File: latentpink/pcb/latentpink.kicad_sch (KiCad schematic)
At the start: 0 parts

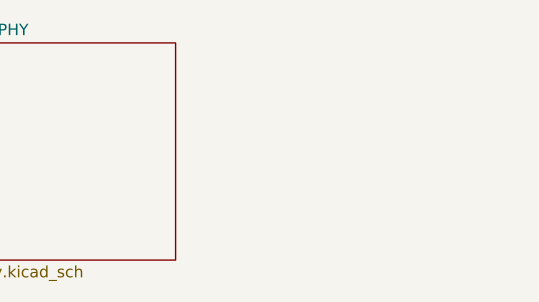
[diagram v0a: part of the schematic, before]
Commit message: Continued initial schematic capture and floorplanning
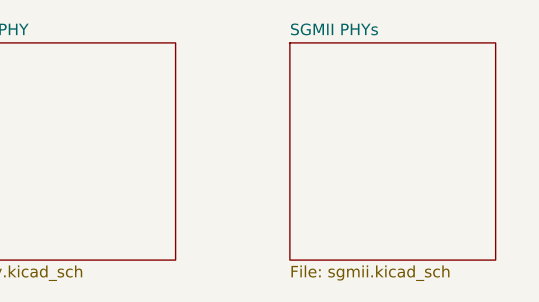
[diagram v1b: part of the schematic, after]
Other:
- added sheet SGMII PHYs (sgmii.kicad_sch)

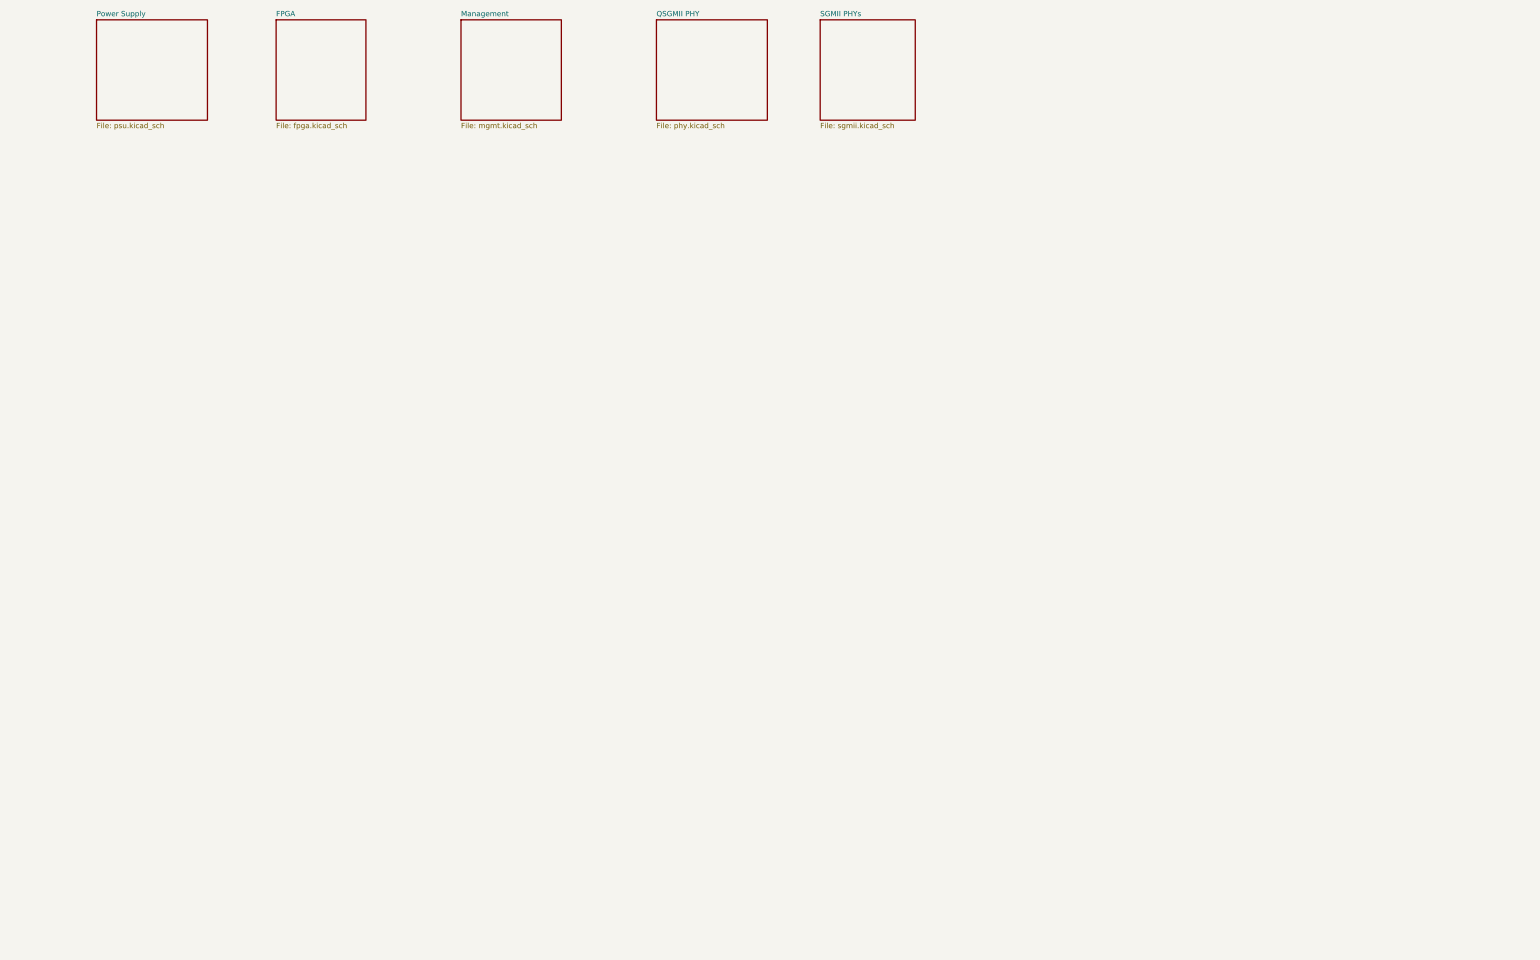
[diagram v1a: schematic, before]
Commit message: Continued initial schematic capture
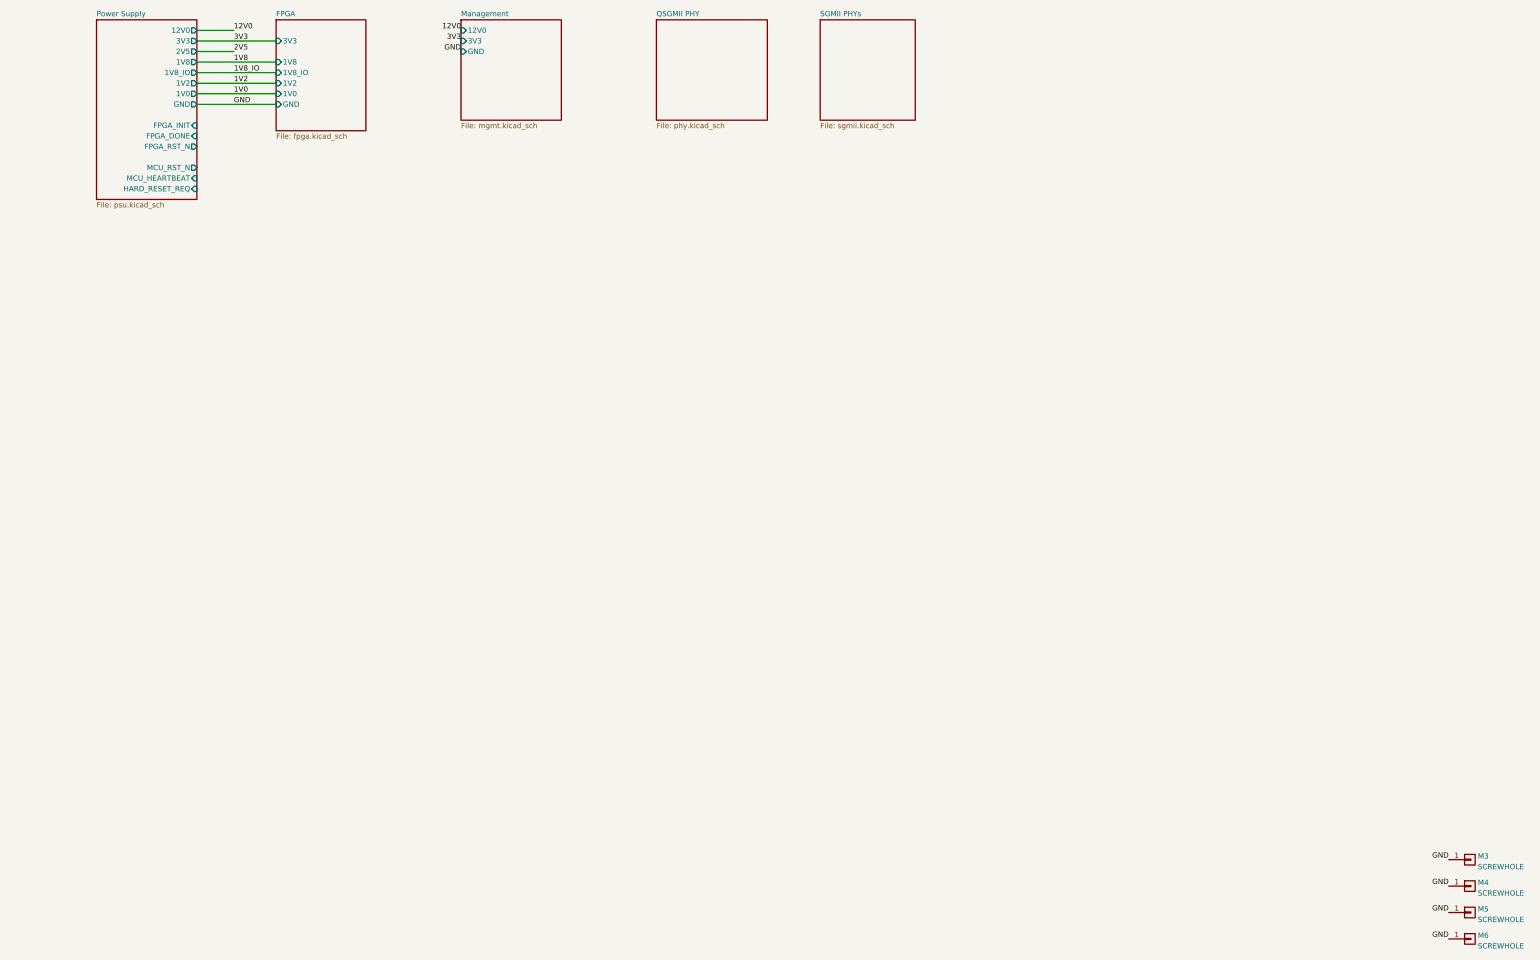
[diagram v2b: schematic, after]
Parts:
- added M3, M4, M5, M6: SCREWHOLE, azonenberg_pcb:MECHANICAL_CLEARANCEHOLE_4_40, symbol conn:CONN_01X01
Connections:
- new net GND: M3.1 (P1), M4.1 (P1), M5.1 (P1), M6.1 (P1)
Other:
- sheet FPGA ports: added 1V0, 1V2, 1V8, 1V8_IO, 3V3, GND; removed none
- sheet Management ports: added 12V0, 3V3, GND; removed none
- sheet Power Supply ports: added 12V0, 1V0, 1V2, 1V8, 1V8_IO, 2V5, 3V3, FPGA_DONE, FPGA_INIT, FPGA_RST_N, GND, HARD_RESET_REQ, MCU_HEARTBEAT, MCU_RST_N; removed none

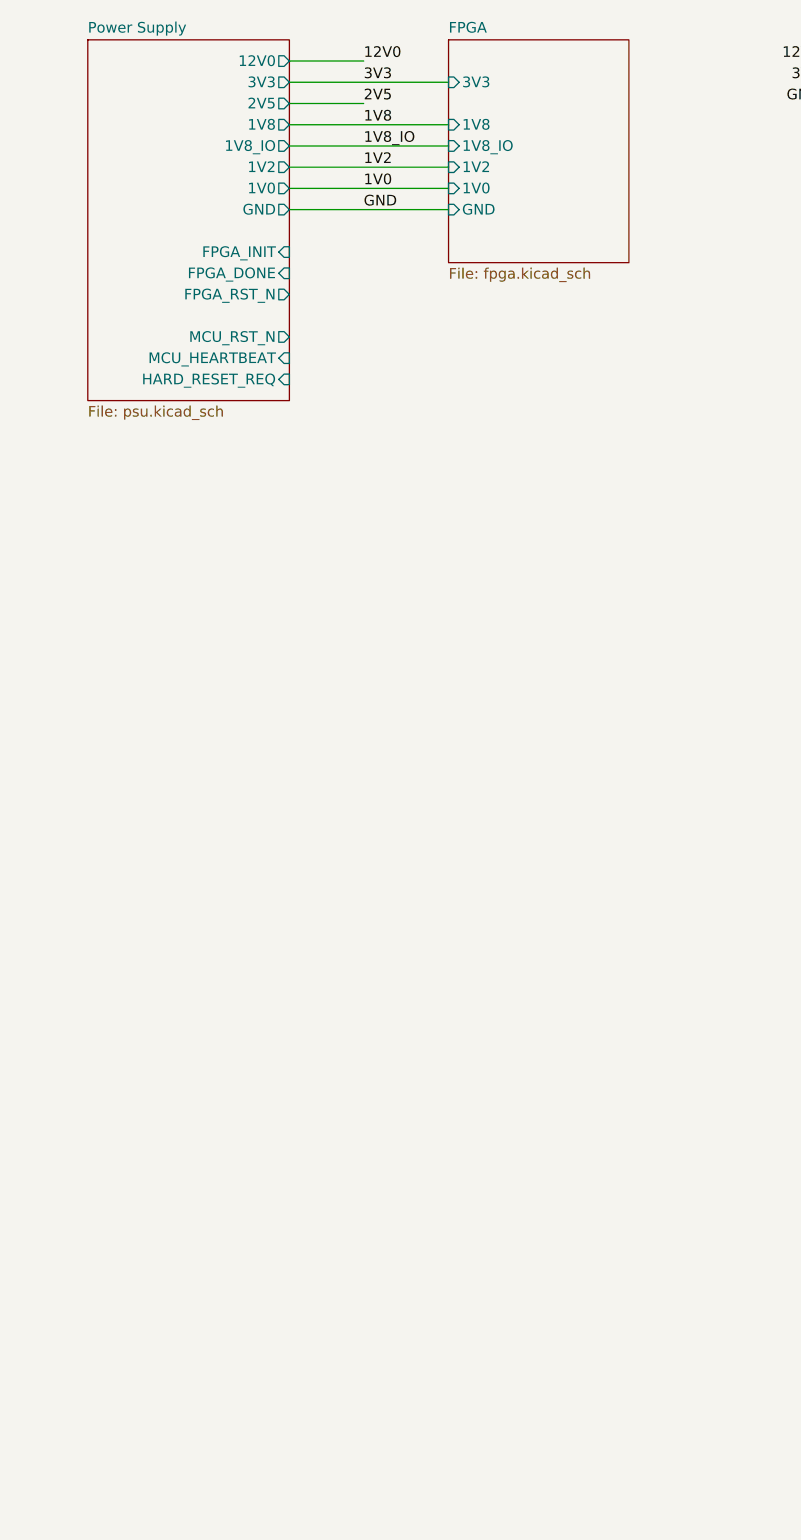
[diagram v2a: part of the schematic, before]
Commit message: Continued work on schematic, mostly power supply and QDR
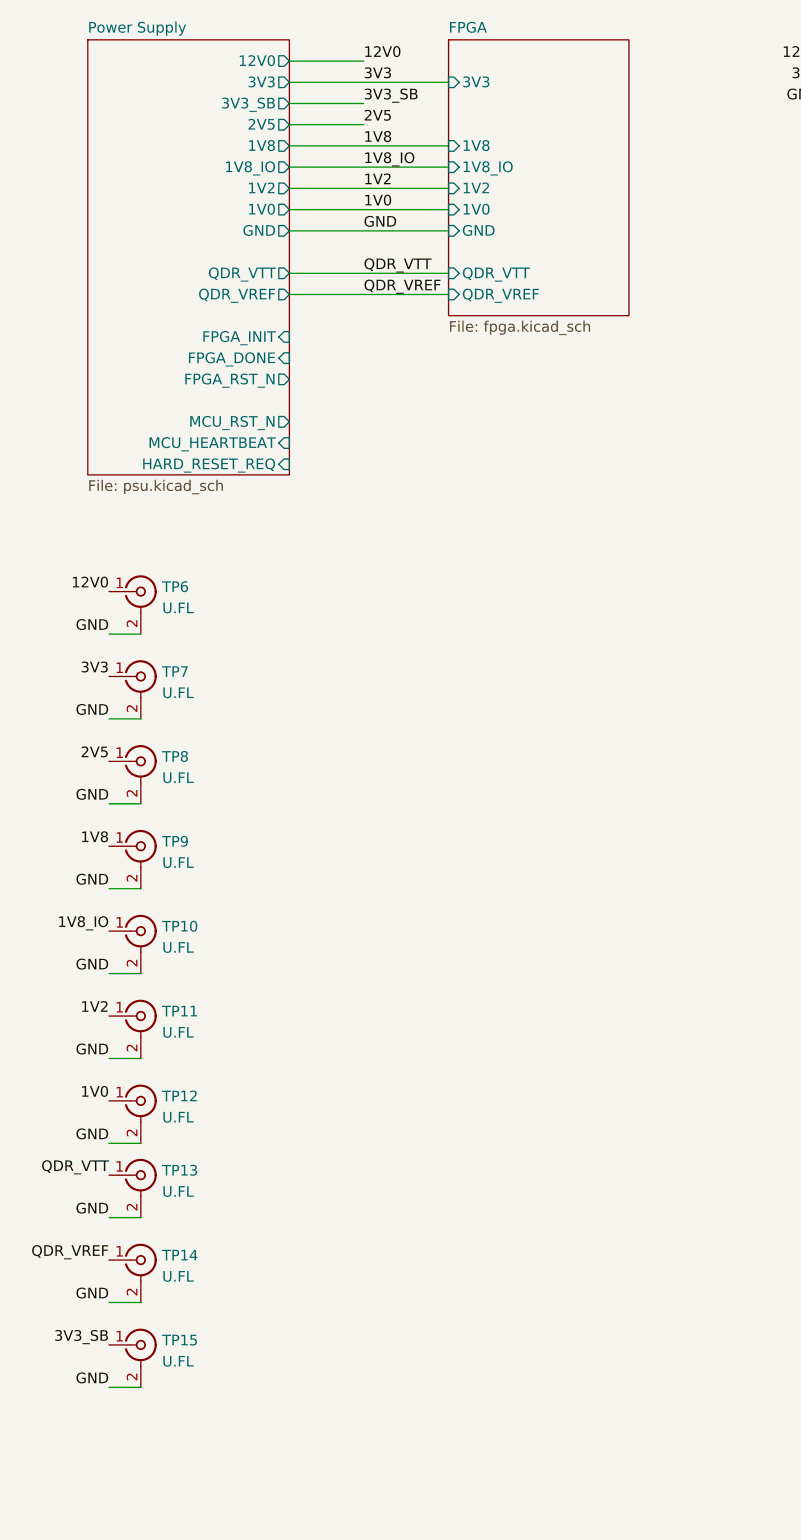
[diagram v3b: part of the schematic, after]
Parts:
- added TP10, TP11, TP12, TP13, TP14, TP15, TP6, TP7, TP8, TP9: U.FL, azonenberg_pcb:CONN_U.FL_TE_1909763-1, symbol conn:CONN_COAXIAL
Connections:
- net 12V0: now also TP6.1 (In)
- net 1V0: now also TP12.1 (In)
- net 1V2: now also TP11.1 (In)
- net 1V8: now also TP9.1 (In)
- net 1V8_IO: now also TP10.1 (In)
- net 2V5: now also TP8.1 (In)
- net 3V3: now also TP7.1 (In)
- net GND: now also TP10.2 (Ext), TP11.2 (Ext), TP12.2 (Ext), TP13.2 (Ext), TP14.2 (Ext), TP15.2 (Ext), TP6.2 (Ext), TP7.2 (Ext), TP8.2 (Ext), TP9.2 (Ext)
- new net 3V3_SB: TP15.1 (In)
- new net QDR_VREF: TP14.1 (In)
- new net QDR_VTT: TP13.1 (In)
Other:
- sheet FPGA ports: added QDR_VREF, QDR_VTT; removed none
- sheet Power Supply ports: added 3V3_SB, QDR_VREF, QDR_VTT; removed none

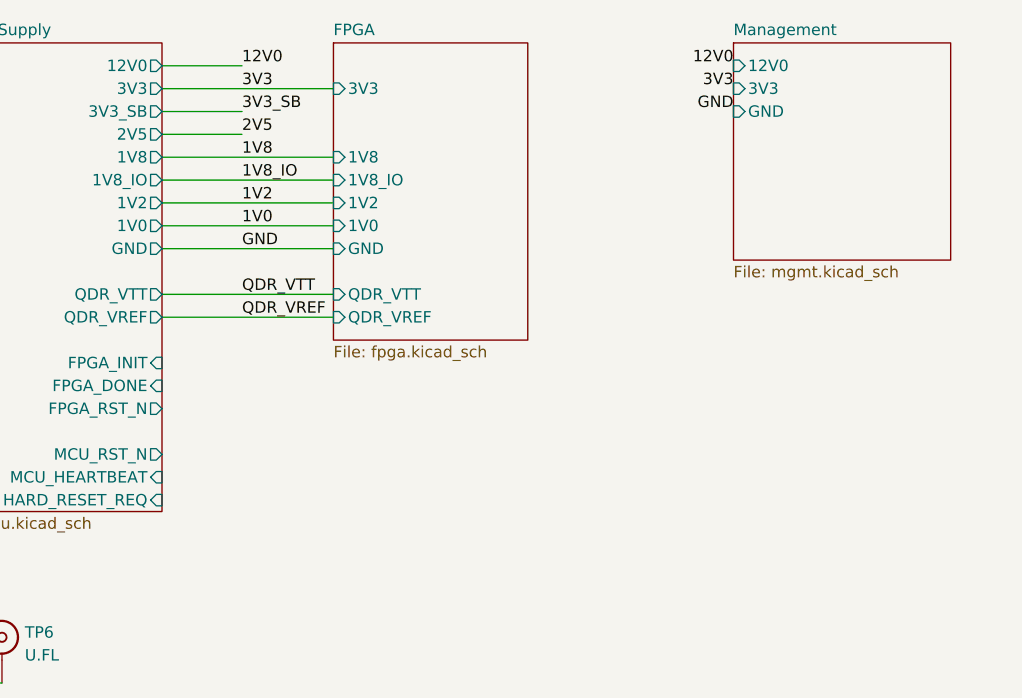
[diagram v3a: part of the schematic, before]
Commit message: Initial version of RGMII PHY schematic
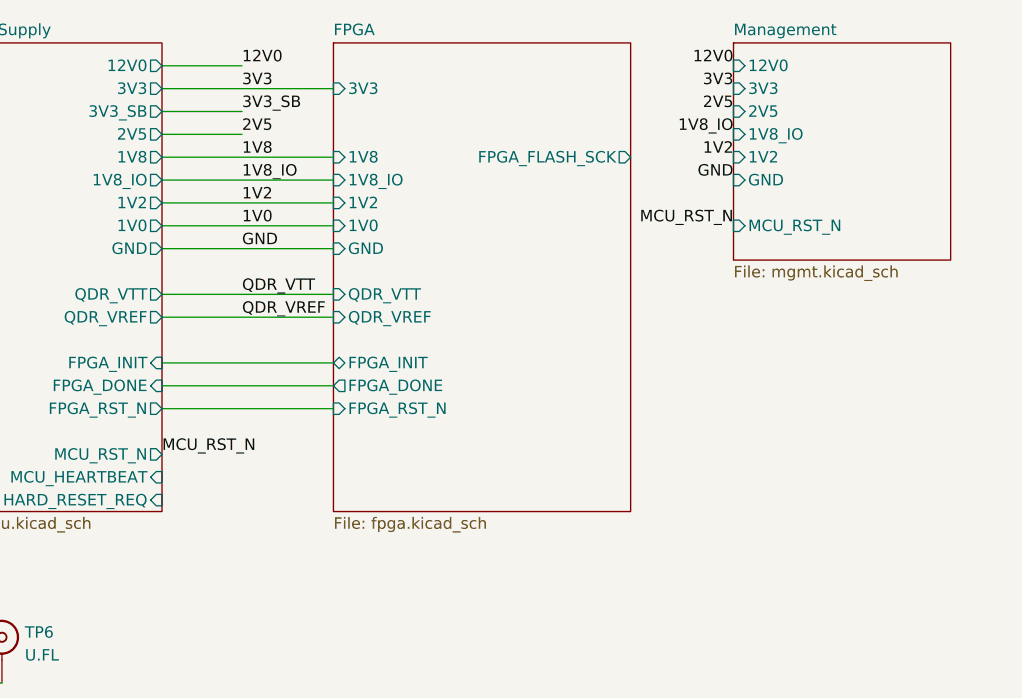
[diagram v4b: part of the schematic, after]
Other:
- sheet FPGA ports: added FPGA_DONE, FPGA_FLASH_SCK, FPGA_INIT, FPGA_RST_N; removed none
- sheet Management ports: added 1V2, 1V8_IO, 2V5, MCU_RST_N; removed none

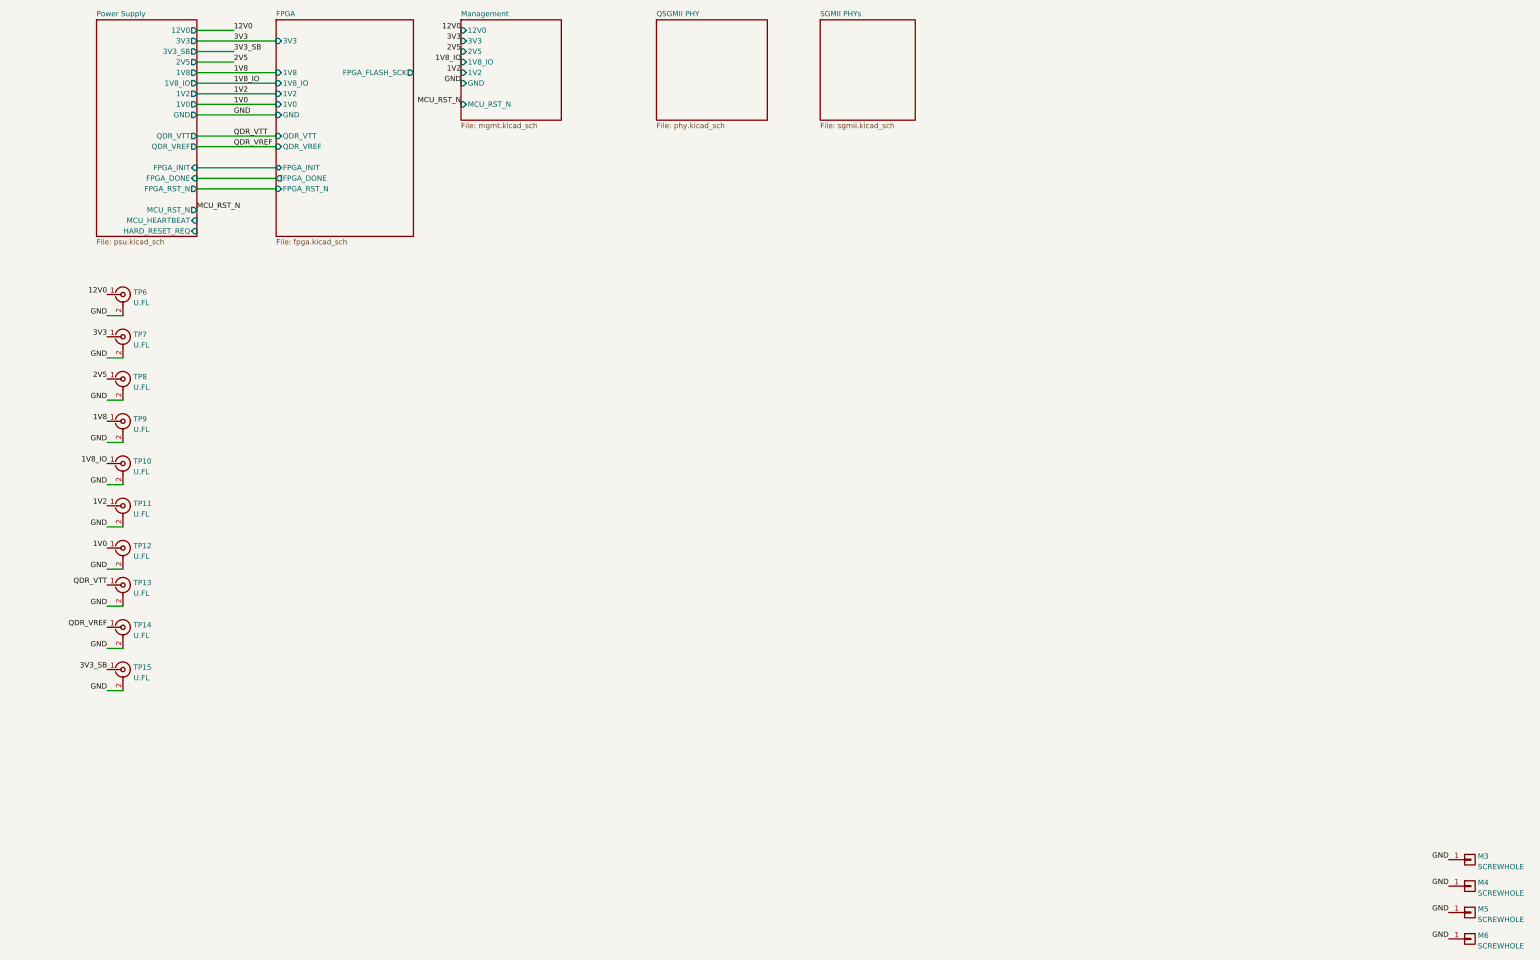
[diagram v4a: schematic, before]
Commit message: Continued work on QSGMII subsystem
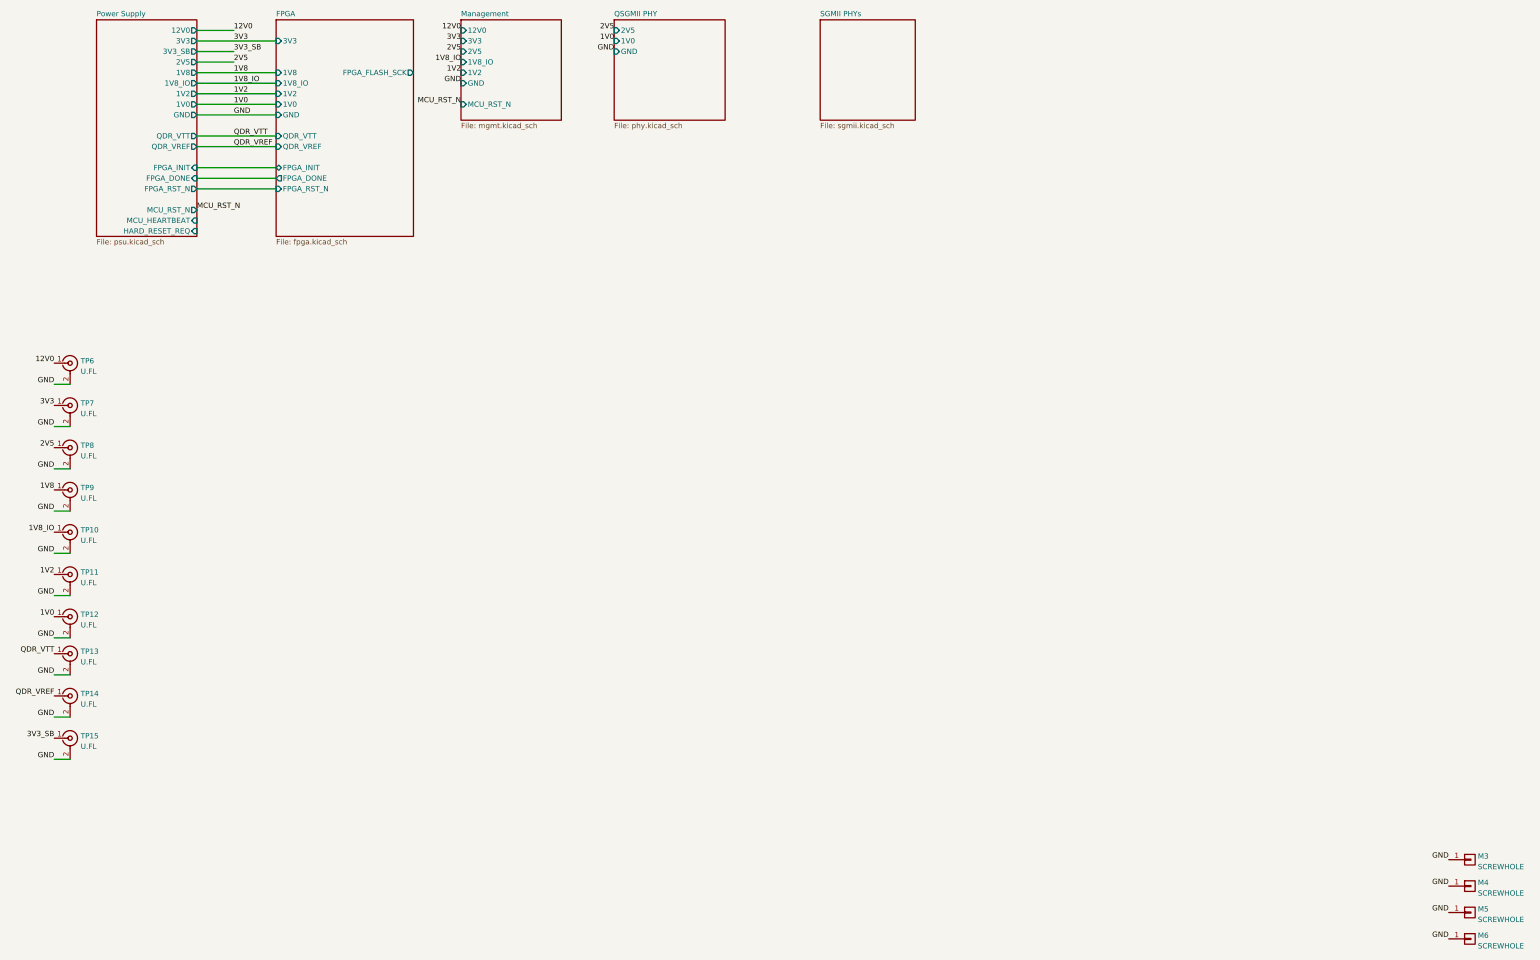
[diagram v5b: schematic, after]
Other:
- sheet QSGMII PHY ports: added 1V0, 2V5, GND; removed none
- moved on the sheet: TP10, TP11, TP12, TP13, TP14, TP15, TP6, TP7, TP8, TP9
